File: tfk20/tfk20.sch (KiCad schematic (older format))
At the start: 14 parts

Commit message: Continue on tfk20
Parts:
- added C? (x2): 1u, symbol Device:C_Small
- added C?: 4.7n, symbol Device:C_Small
- added D?: D_Small, symbol Device:D_Small
- added J?: Conn_01x06_Male, symbol Connector:Conn_01x06_Male
- added R?: 1M, symbol Device:R_Small
- added R?: 1.5k, symbol Device:R_Small
- added U?: USBLC6-2SC6, Package_TO_SOT_SMD:SOT-23-6, symbol Power_Protection:USBLC6-2SC6
- U?: value STM32F042K6Tx -> STM32F042K6T6
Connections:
- net labels added: CASE
- wire segments 124 -> 151
- no-connect marks 11 -> 12
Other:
- note added: "Decoupling capacitors for MCU (Figure 13, p. 43)\nImportant: Must be close to MCU on PCB"
- note added: "ESD inrush protection"
- note added: "Pull-up indicates \nUSB 1.1 Full Speed"
- note added: "SWD Debug Port"
- note added: "Upstream facing port \ntermination"
- moved on the sheet: C?, J?, R?, U?

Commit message: RGB LED driver
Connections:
- net labels added: SPI_MISO, SPI_MOSI, SPI_SCK
- net labels removed: RGB_MATRIX
- wire segments 151 -> 143
- no-connect marks 12 -> 10
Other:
- note added: "Key and LED sub-sheets"
- note added: "Linear voltage regulator"
- note added: "MCU"
- note added: "USB-C"
- moved on the sheet: C?, D?, J?, R?, U?

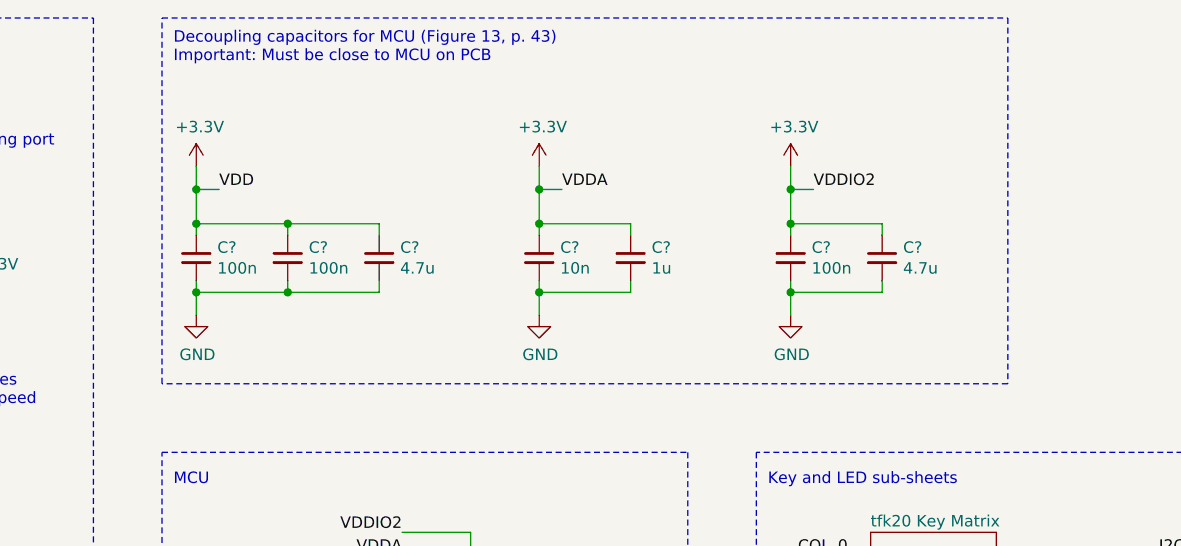
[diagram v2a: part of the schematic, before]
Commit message: Change caps layout
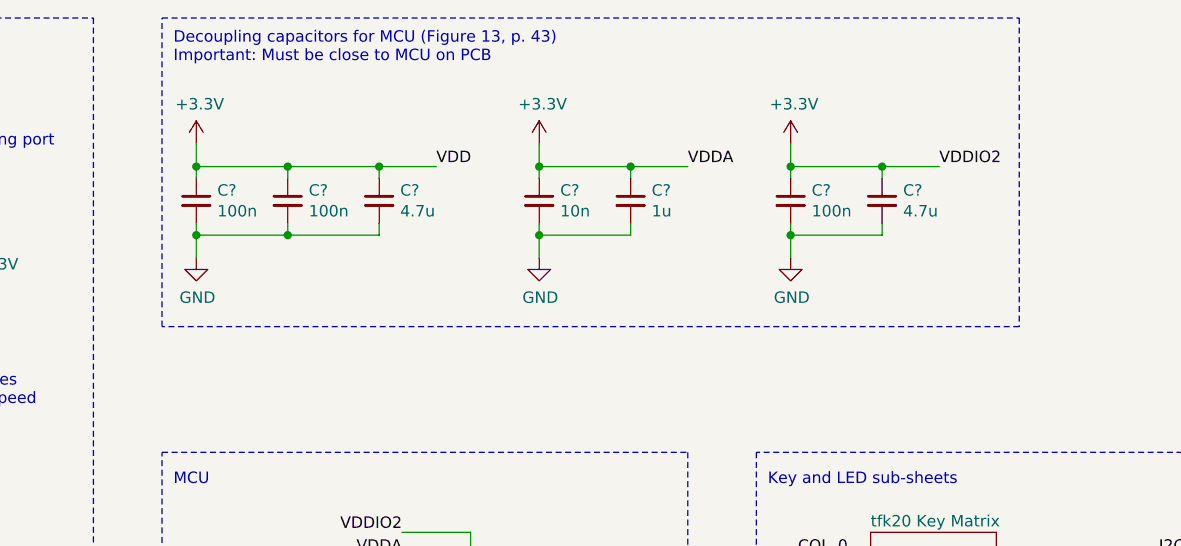
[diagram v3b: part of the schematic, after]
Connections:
- wire segments 143 -> 140
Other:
- moved on the sheet: C?
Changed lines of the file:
@@
 L Device:C_Small C?
 U 1 1 601952A7
-P 4750 1750
-F 0 "C?" H 4842 1796 50  0000 L CNN
-F 1 "100n" H 4842 1705 50  0000 L CNN
-F 2 "" H 4750 1750 50  0001 C CNN
-F 3 "~" H 4750 1750 50  0001 C CNN
-	1    4750 1750
+P 4750 1500
+F 0 "C?" H 4842 1546 50  0000 L CNN
+F 1 "100n" H 4842 1455 50  0000 L CNN
+F 2 "" H 4750 1500 50  0001 C CNN
+F 3 "~" H 4750 1500 50  0001 C CNN
+	1    4750 1500
 	1    0    0    -1
 $EndComp
@@
 L Device:C_Small C?
 U 1 1 6019567A
-P 5150 1750
-F 0 "C?" H 5242 1796 50  0000 L CNN
-F 1 "4.7u" H 5242 1705 50  0000 L CNN
-F 2 "" H 5150 1750 50  0001 C CNN
-F 3 "~" H 5150 1750 50  0001 C CNN
-	1    5150 1750
+P 5150 1500
+F 0 "C?" H 5242 1546 50  0000 L CNN
+F 1 "4.7u" H 5242 1455 50  0000 L CNN
+F 2 "" H 5150 1500 50  0001 C CNN
+F 3 "~" H 5150 1500 50  0001 C CNN
+	1    5150 1500
 	1    0    0    -1
 $EndComp
@@
 L Device:C_Small C?
 U 1 1 60195F04
-P 4350 1750
-F 0 "C?" H 4442 1796 50  0000 L CNN
-F 1 "100n" H 4442 1705 50  0000 L CNN
-F 2 "" H 4350 1750 50  0001 C CNN
-F 3 "~" H 4350 1750 50  0001 C CNN
-	1    4350 1750
+P 4350 1500
+F 0 "C?" H 4442 1546 50  0000 L CNN
+F 1 "100n" H 4442 1455 50  0000 L CNN
+F 2 "" H 4350 1500 50  0001 C CNN
+F 3 "~" H 4350 1500 50  0001 C CNN
+	1    4350 1500
 	1    0    0    -1
 $EndComp
@@
 L Device:C_Small C?
 U 1 1 60196A16
-P 6950 1750
-F 0 "C?" H 7042 1796 50  0000 L CNN
-F 1 "100n" H 7042 1705 50  0000 L CNN
-F 2 "" H 6950 1750 50  0001 C CNN
-F 3 "~" H 6950 1750 50  0001 C CNN
-	1    6950 1750
+P 6950 1500
+F 0 "C?" H 7042 1546 50  0000 L CNN
+F 1 "100n" H 7042 1455 50  0000 L CNN
+F 2 "" H 6950 1500 50  0001 C CNN
+F 3 "~" H 6950 1500 50  0001 C CNN
+	1    6950 1500
 	1    0    0    -1
 $EndComp
@@
 L Device:C_Small C?
 U 1 1 60196A1C
-P 7350 1750
-F 0 "C?" H 7442 1796 50  0000 L CNN
-F 1 "4.7u" H 7442 1705 50  0000 L CNN
-F 2 "" H 7350 1750 50  0001 C CNN
-F 3 "~" H 7350 1750 50  0001 C CNN
-	1    7350 1750
+P 7350 1500
+F 0 "C?" H 7442 1546 50  0000 L CNN
+F 1 "4.7u" H 7442 1455 50  0000 L CNN
+F 2 "" H 7350 1500 50  0001 C CNN
+F 3 "~" H 7350 1500 50  0001 C CNN
+	1    7350 1500
 	1    0    0    -1
 $EndComp
@@
 L Device:C_Small C?
 U 1 1 601970AA
-P 5850 1750
-F 0 "C?" H 5942 1796 50  0000 L CNN
-F 1 "10n" H 5942 1705 50  0000 L CNN
-F 2 "" H 5850 1750 50  0001 C CNN
-F 3 "~" H 5850 1750 50  0001 C CNN
-	1    5850 1750
+P 5850 1500
+F 0 "C?" H 5942 1546 50  0000 L CNN
+F 1 "10n" H 5942 1455 50  0000 L CNN
+F 2 "" H 5850 1500 50  0001 C CNN
+F 3 "~" H 5850 1500 50  0001 C CNN
+	1    5850 1500
 	1    0    0    -1
 $EndComp
@@
 L Device:C_Small C?
 U 1 1 601970B0
-P 6250 1750
-F 0 "C?" H 6342 1796 50  0000 L CNN
-F 1 "1u" H 6342 1705 50  0000 L CNN
-F 2 "" H 6250 1750 50  0001 C CNN
-F 3 "~" H 6250 1750 50  0001 C CNN
-	1    6250 1750
-	1    0    0    -1
-$EndComp
-Wire Wire Line
-	6950 1850 6950 1900
-Wire Wire Line
-	6950 1900 7350 1900
-Wire Wire Line
-	7350 1900 7350 1850
-Wire Wire Line
-	6950 1600 7350 1600
-Wire Wire Line
-	7350 1600 7350 1650
-Wire Wire Line
-	6950 1650 6950 1600
-Connection ~ 6950 1600
-Connection ~ 6950 1900
-Wire Wire Line
-	6950 1350 6950 1450
+P 6250 1500
+F 0 "C?" H 6342 1546 50  0000 L CNN
+F 1 "1u" H 6342 1455 50  0000 L CNN
+F 2 "" H 6250 1500 50  0001 C CNN
+F 3 "~" H 6250 1500 50  0001 C CNN
+	1    6250 1500
+	1    0    0    -1
+$EndComp
+Wire Wire Line
+	6950 1600 6950 1650
+Wire Wire Line
+	6950 1650 7350 1650
+Wire Wire Line
+	7350 1650 7350 1600
+Wire Wire Line
+	6950 1350 7350 1350
+Wire Wire Line
+	7350 1350 7350 1400
+Wire Wire Line
+	6950 1400 6950 1350
+Connection ~ 6950 1350
+Connection ~ 6950 1650
 $Comp
 L power:+3.3V #PWR0101
 U 1 1 6019D23A
-P 6950 1350
-F 0 "#PWR0101" H 6950 1200 50  0001 C CNN
-F 1 "+3.3V" H 6965 1523 50  0000 C CNN
-F 2 "" H 6950 1350 50  0001 C CNN
-F 3 "" H 6950 1350 50  0001 C CNN
-	1    6950 1350
-	1    0    0    -1
-$EndComp
-Text Label 7050 1450 0    50   ~ 0
+P 6950 1250
+F 0 "#PWR0101" H 6950 1100 50  0001 C CNN
+F 1 "+3.3V" H 6965 1423 50  0000 C CNN
+F 2 "" H 6950 1250 50  0001 C CNN
+F 3 "" H 6950 1250 50  0001 C CNN
+	1    6950 1250
+	1    0    0    -1
+$EndComp
+Text Label 7600 1350 0    50   ~ 0
 VDDIO2
 Wire Wire Line
-	6950 1900 6950 2000
+	6950 1650 6950 1750
+Wire Wire Line
+	5850 1400 5850 1350
+Wire Wire Line
+	5850 1350 6250 1350
+Wire Wire Line
+	6250 1350 6250 1400
+Wire Wire Line
+	6250 1600 6250 1650
+Wire Wire Line
+	6250 1650 5850 1650
 Wire Wire Line
 	5850 1650 5850 1600
-Wire Wire Line
-	5850 1600 6250 1600
-Wire Wire Line
-	6250 1600 6250 1650
-Wire Wire Line
-	6250 1850 6250 1900
-Wire Wire Line
-	6250 1900 5850 1900
-Wire Wire Line
-	5850 1900 5850 1850
 $Comp
 L power:+3.3V #PWR0102
 U 1 1 601A1F07
-P 5850 1350
-F 0 "#PWR0102" H 5850 1200 50  0001 C CNN
-F 1 "+3.3V" H 5865 1523 50  0000 C CNN
-F 2 "" H 5850 1350 50  0001 C CNN
-F 3 "" H 5850 1350 50  0001 C CNN
-	1    5850 1350
-	1    0    0    -1
-$EndComp
-Text Label 5950 1450 0    50   ~ 0
+P 5850 1250
+F 0 "#PWR0102" H 5850 1100 50  0001 C CNN
+F 1 "+3.3V" H 5865 1423 50  0000 C CNN
+F 2 "" H 5850 1250 50  0001 C CNN
+F 3 "" H 5850 1250 50  0001 C CNN
+	1    5850 1250
+	1    0    0    -1
+$EndComp
+Text Label 6500 1350 0    50   ~ 0
 VDDA
-Connection ~ 5850 1600
-Connection ~ 5850 1900
-Wire Wire Line
-	5850 1350 5850 1450
-Wire Wire Line
-	5850 1900 5850 2000
+Connection ~ 5850 1350
+Connection ~ 5850 1650
+Wire Wire Line
+	5850 1650 5850 1750
+Wire Wire Line
+	4350 1400 4350 1350
+Wire Wire Line
+	4350 1350 4750 1350
+Wire Wire Line
+	4750 1350 4750 1400
+Wire Wire Line
+	4750 1350 5150 1350
+Wire Wire Line
+	5150 1350 5150 1400
+Connection ~ 4750 1350
+Wire Wire Line
+	5150 1600 5150 1650
+Wire Wire Line
+	5150 1650 4750 1650
+Wire Wire Line
+	4750 1650 4750 1600
+Wire Wire Line
+	4750 1650 4350 1650
 Wire Wire Line
 	4350 1650 4350 1600
-Wire Wire Line
-	4350 1600 4750 1600
-Wire Wire Line
-	4750 1600 4750 1650
-Wire Wire Line
-	4750 1600 5150 1600
-Wire Wire Line
-	5150 1600 5150 1650
-Connection ~ 4750 1600
-Wire Wire Line
-	5150 1850 5150 1900
-Wire Wire Line
-	5150 1900 4750 1900
-Wire Wire Line
-	4750 1900 4750 1850
-Wire Wire Line
-	4750 1900 4350 1900
-Wire Wire Line
-	4350 1900 4350 1850
-Connection ~ 4750 1900
-Connection ~ 4350 1600
-Connection ~ 4350 1900
-Wire Wire Line
-	4350 1600 4350 1450
+Connection ~ 4750 1650
+Connection ~ 4350 1350
+Connection ~ 4350 1650
 $Comp
 L power:+3.3V #PWR0103
 U 1 1 601A9EEA
-P 4350 1350
-F 0 "#PWR0103" H 4350 1200 50  0001 C CNN
-F 1 "+3.3V" H 4365 1523 50  0000 C CNN
-F 2 "" H 4350 1350 50  0001 C CNN
-F 3 "" H 4350 1350 50  0001 C CNN
-	1    4350 1350
-	1    0    0    -1
-$EndComp
-Text Label 4450 1450 0    50   ~ 0
+P 4350 1250
+F 0 "#PWR0103" H 4350 1100 50  0001 C CNN
+F 1 "+3.3V" H 4365 1423 50  0000 C CNN
+F 2 "" H 4350 1250 50  0001 C CNN
+F 3 "" H 4350 1250 50  0001 C CNN
+	1    4350 1250
+	1    0    0    -1
+$EndComp
+Text Label 5400 1350 0    50   ~ 0
 VDD
 Wire Wire Line
@@
 RGB_LIGHT
 Wire Wire Line
-	4350 1450 4450 1450
-Connection ~ 4350 1450
-Wire Wire Line
-	4350 1450 4350 1350
-Wire Wire Line
-	4350 1900 4350 2000
+	4350 1650 4350 1750
 $Comp
 L power:GND #PWR0112
 U 1 1 601DC47E
-P 4350 2000
-F 0 "#PWR0112" H 4350 1750 50  0001 C CNN
-F 1 "GND" H 4355 1827 50  0000 C CNN
-F 2 "" H 4350 2000 50  0001 C CNN
-F 3 "" H 4350 2000 50  0001 C CNN
-	1    4350 2000
-	1    0    0    -1
-$EndComp
-Wire Wire Line
-	5950 1450 5850 1450
-Connection ~ 5850 1450
-Wire Wire Line
-	5850 1450 5850 1600
+P 4350 1750
+F 0 "#PWR0112" H 4350 1500 50  0001 C CNN
+F 1 "GND" H 4355 1577 50  0000 C CNN
+F 2 "" H 4350 1750 50  0001 C CNN
+F 3 "" H 4350 1750 50  0001 C CNN
+	1    4350 1750
+	1    0    0    -1
+$EndComp
 $Comp
 L power:GND #PWR0113
 U 1 1 601EDF93
-P 5850 2000
-F 0 "#PWR0113" H 5850 1750 50  0001 C CNN
-F 1 "GND" H 5855 1827 50  0000 C CNN
-F 2 "" H 5850 2000 50  0001 C CNN
-F 3 "" H 5850 2000 50  0001 C CNN
-	1    5850 2000
-	1    0    0    -1
-$EndComp
-Wire Wire Line
-	7050 1450 6950 1450
-Connection ~ 6950 1450
-Wire Wire Line
-	6950 1450 6950 1600
+P 5850 1750
+F 0 "#PWR0113" H 5850 1500 50  0001 C CNN
+F 1 "GND" H 5855 1577 50  0000 C CNN
+F 2 "" H 5850 1750 50  0001 C CNN
+F 3 "" H 5850 1750 50  0001 C CNN
+	1    5850 1750
+	1    0    0    -1
+$EndComp
 $Comp
 L power:GND #PWR0114
 U 1 1 601FFA12
-P 6950 2000
-F 0 "#PWR0114" H 6950 1750 50  0001 C CNN
-F 1 "GND" H 6955 1827 50  0000 C CNN
-F 2 "" H 6950 2000 50  0001 C CNN
-F 3 "" H 6950 2000 50  0001 C CNN
-	1    6950 2000
+P 6950 1750
+F 0 "#PWR0114" H 6950 1500 50  0001 C CNN
+F 1 "GND" H 6955 1577 50  0000 C CNN
+F 2 "" H 6950 1750 50  0001 C CNN
+F 3 "" H 6950 1750 50  0001 C CNN
+	1    6950 1750
 	1    0    0    -1
 $EndComp
@@
 SPI_MOSI
 Wire Notes Line
-	4200 700  7900 700
-Wire Notes Line
-	7900 700  7900 2300
-Wire Notes Line
-	7900 2300 4200 2300
-Wire Notes Line
-	4200 2300 4200 700
+	4200 700  7950 700
+Wire Notes Line
+	7950 700  7950 2050
+Wire Notes Line
+	7950 2050 4200 2050
+Wire Notes Line
+	4200 2050 4200 700
 Text Notes 4250 2750 0    50   ~ 0
 MCU
@@
 Wire Notes Line
 	7150 6000 7150 4750
+Wire Wire Line
+	4350 1250 4350 1350
+Wire Wire Line
+	5850 1250 5850 1350
+Wire Wire Line
+	6950 1250 6950 1350
+Wire Wire Line
+	5150 1350 5400 1350
+Connection ~ 5150 1350
+Wire Wire Line
+	6250 1350 6500 1350
+Connection ~ 6250 1350
+Wire Wire Line
+	7350 1350 7600 1350
+Connection ~ 7350 1350
 $EndSCHEMATC

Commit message: Change MCU, add another row, add reset button
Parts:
- removed U?: STM32F042K6T6, Package_QFP:LQFP-32_7x7mm_P0.8mm, symbol MCU_ST_STM32F0:STM32F042K6Tx
- added C4: 10u, symbol Device:C_Small
- added C5, C7: 4.7n, symbol Device:C_Small
- added D1: D_Small, symbol Device:D_Small
- added F1: 500mA, symbol Device:Polyfuse_Small
- added H1: Case, symbol Mechanical:MountingHole_Pad
- added Q1: DTC123J, symbol Transistor_BJT:DTC123J
- added R2: 100k, symbol Device:R_Small
- added R7, R8: 22, symbol Device:R_Small
- added SW1: Reset, symbol Switch:SW_Push
- added U3: STM32F072CBTx, Package_QFP:LQFP-48_7x7mm_P0.5mm, symbol MCU_ST_STM32F0:STM32F072CBTx
- gave numbers to parts that had none: 21
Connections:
- net labels added: BOOT0, I2C2_SCL, I2C2_SDA, IN_USB_D+, IN_USB_D-, ROW_5, SHIELD
- net labels removed: CASE
- wire segments 140 -> 210
- no-connect marks 10 -> 28
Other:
- note added: "Data line termination \nresistors for D+ and D-"
- note added: "Decoupling capacitors for MCU (Figure 13, p. 49, DS9826)\nImportant: Must be close to MCU on PCB"
- note added: "ERC power flags"
- note added: "Keep ESD away from GND and ICs, \nso shunt to USB shield."
- note added: "PA7 is next to \nPB0 on LQFP48\n"
- note added: "Pull-up indicates \nUSB Full Speed"
- note added: "Reset and flash button"
- note added: "Resets MCU and pulls BOOT0 high\non fourth rising edge after reset.\nThis puts the MCU into bootloader \nmode to reprogram via USB DFU.\nSee ST RM0091 (pp. 52)."
- note added: "TODO: Overvoltage \nprotection with \nZener/Schottky diode"
- note added: "USB data and VBUS ESD protection"
- note removed: "Decoupling capacitors for MCU (Figure 13, p. 43)\nImportant: Must be close to MCU on PCB"
- note removed: "Pull-up indicates \nUSB 1.1 Full Speed"
- moved on the sheet: C1, C10, C11, C12, C13, C14, C2, C3, C6, C8, C9, D2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
